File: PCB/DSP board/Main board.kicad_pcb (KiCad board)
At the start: 4 copper layers, 60 x 100 mm, 195 parts, among them J201 01x06 male SMD, J701 Conn_01x40_Female, J702 Conn_01x06_Female, J801 1140084168, J901 USB_B, U201 STM32H743II, U401 AS4C32M8SA, U501 CS42448, U601 MIC23050, U602 TPS2113A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

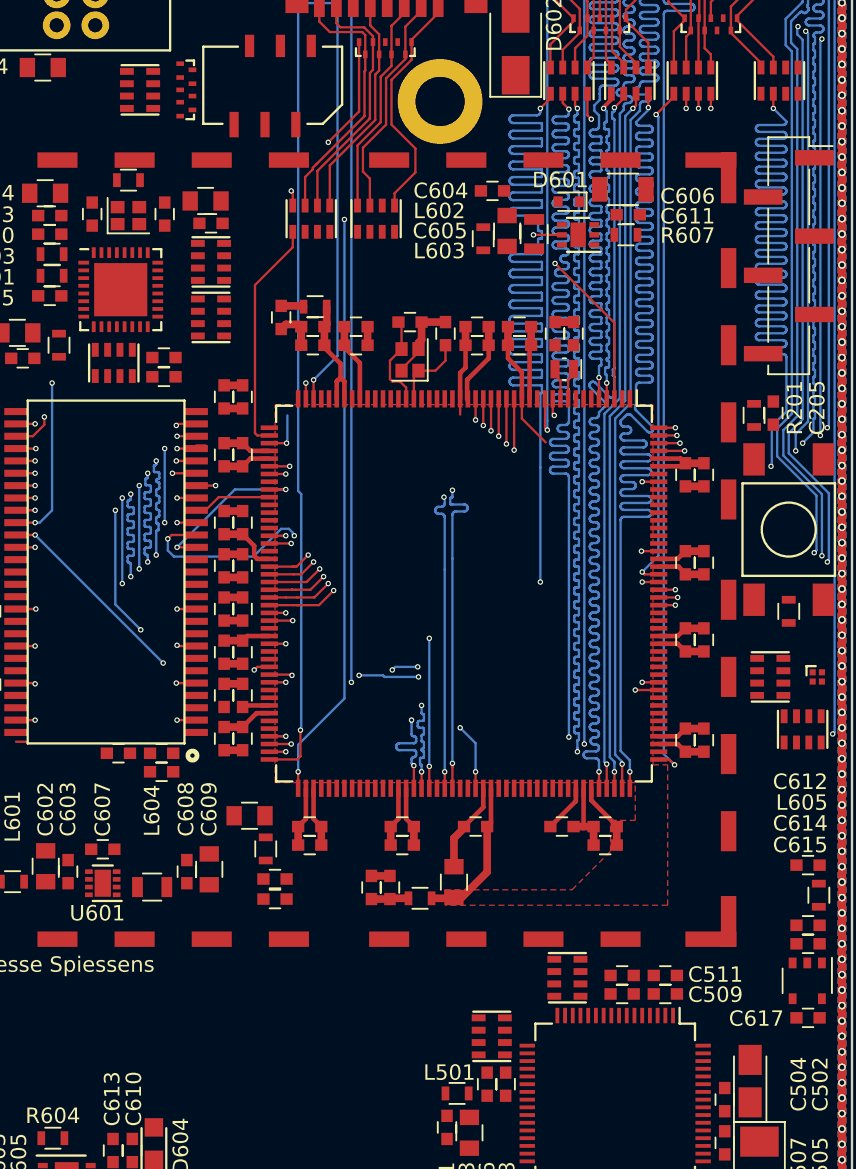
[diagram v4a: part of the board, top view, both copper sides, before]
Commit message: High Speed routing
High speed routing (USB, SDMMC, CODEC, RAM and Screen) are hooked up
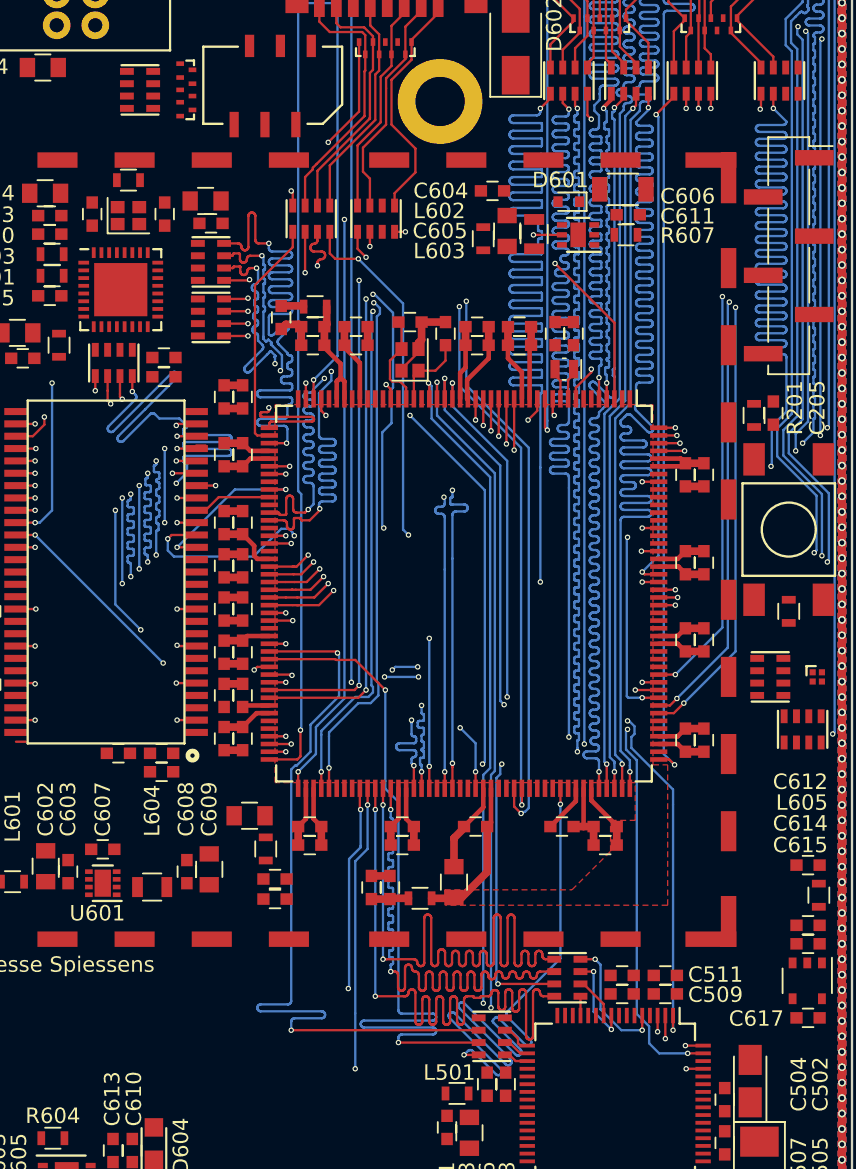
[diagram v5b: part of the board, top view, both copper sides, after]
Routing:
- net SPI5_MISO: track 0.00 -> 58.1 mm, vias 0 -> 3
- net SPI5_MOSI: track 0.00 -> 57.5 mm, vias 0 -> 3
- net SPI5_SCK: track 0.00 -> 57.5 mm, vias 0 -> 4
- net SDMMC1_D1: track 0.00 -> 55.0 mm, vias 0 -> 3
- net SDMMC1_D3: track 0.00 -> 54.7 mm, vias 0 -> 3
- net SDMMC1_CMD: track 0.00 -> 54.7 mm, vias 0 -> 3
- net SDMMC1_D2: track 0.00 -> 54.7 mm, vias 0 -> 3
- net SDMMC1_D0: track 0.00 -> 54.6 mm, vias 0 -> 3
- net SPI5_NSS: track 0.00 -> 53.7 mm, vias 0 -> 4
- net SAI2_FS_B: track 0.00 -> 50.7 mm, vias 0 -> 2
- net SAI2_FS_A: track 0.00 -> 50.7 mm, vias 0 -> 2
- net SAI2_MCK_B: track 0.00 -> 50.7 mm, vias 0 -> 5
- net SAI2_SCK_B: track 0.00 -> 50.7 mm, vias 0 -> 2
- net SAI2_SD_B: track 0.00 -> 50.7 mm, vias 0 -> 2
- net SAI2_SD_A: track 0.00 -> 50.5 mm, vias 0 -> 2
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
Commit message: PCI almost routed
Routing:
- net ADC123_INP11: track 0.00 -> 84.0 mm, vias 0 -> 8
- net ADC1_INP16: track 0.00 -> 83.7 mm, vias 0 -> 7
- net ADC3_INP6: track 0.00 -> 80.5 mm, vias 0 -> 7
- net COMP_1_INP: track 0.00 -> 76.3 mm, vias 0 -> 6
- net COMP_1_OUT: track 0.00 -> 75.4 mm, vias 0 -> 5
- net DAC1_OUT1: track 1.32 -> 76.5 mm, vias 1 -> 9
- net ADC12_INP3: track 0.00 -> 66.5 mm, vias 0 -> 2
- net HRTIM_EEV3: track 0.00 -> 62.9 mm, vias 0 -> 12
- net HRTIM_FLT3: track 0.00 -> 61.2 mm, vias 0 -> 8
- net MCO1: track 0.00 -> 53.7 mm, vias 0 -> 6
- net SPI2_SCK: track 0.00 -> 51.7 mm, vias 0 -> 5
- net HRTIM_CHE1: track 0.00 -> 44.1 mm, vias 0 -> 4
- net NRST: track 0.00 -> 40.1 mm, vias 0 -> 3
- net SPI2_MOSI: track 0.00 -> 39.7 mm, vias 0 -> 5
- net SPDIFRX_IN1: track 0.00 -> 39.4 mm, vias 0 -> 2
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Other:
- rule via_min_size: 0.3524 -> 0.35

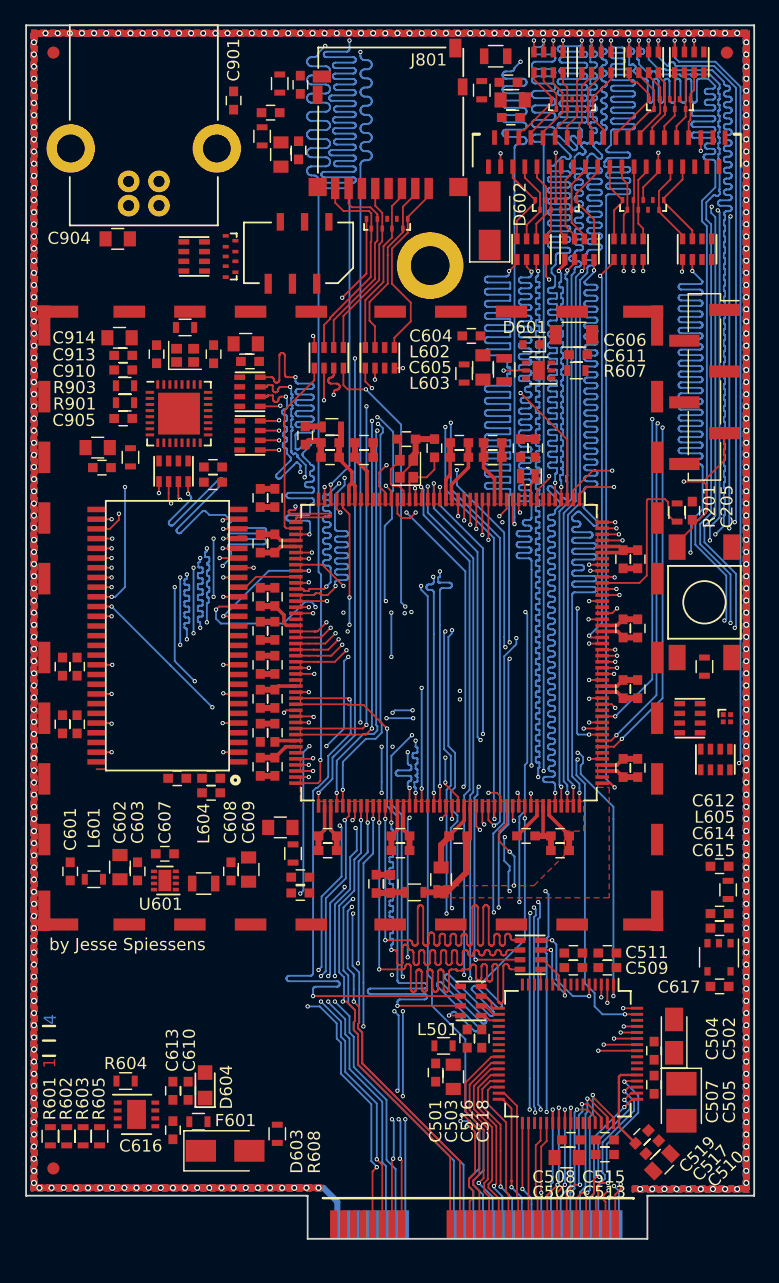
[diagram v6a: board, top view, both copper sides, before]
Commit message: Almost done routing
20 connections to be made.
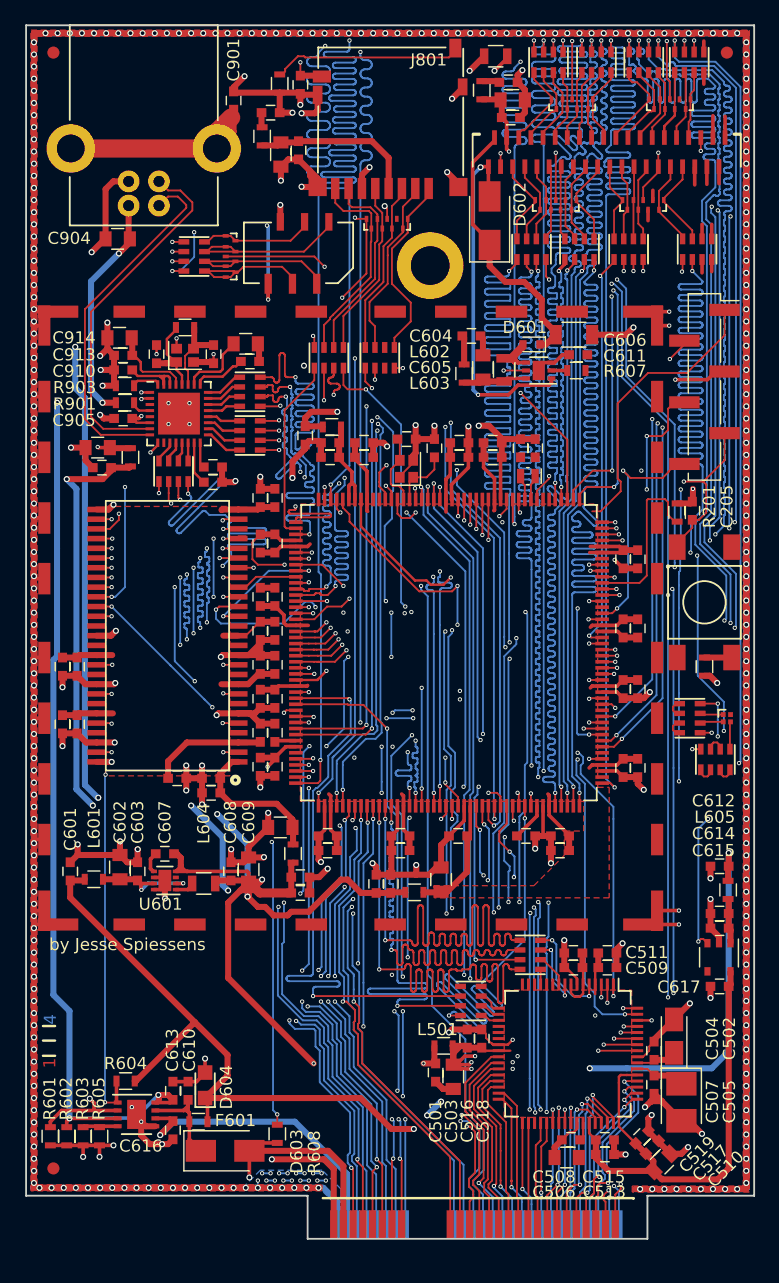
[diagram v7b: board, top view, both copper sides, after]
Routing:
- net GND: track 928.5 -> 1256.2 mm, vias 285 -> 406
- net +3V3: track 3.89 -> 212.3 mm, vias 0 -> 13
- net VBUS: track 0.00 -> 121.2 mm, vias 0 -> 6
- net +5V: track 0.00 -> 102.0 mm, vias 0 -> 5
- net I2C4_SDA: track 1.18 -> 92.7 mm, vias 1 -> 6
- net I2C4_SCL: track 1.43 -> 89.8 mm, vias 1 -> 4
- net I2C1_SCL: track 1.05 -> 75.1 mm, vias 1 -> 5
- net I2C1_SDA: track 0.97 -> 73.3 mm, vias 1 -> 4
- net TOUCH_NRESET: track 3.53 -> 61.5 mm, vias 1 -> 3
- net SPI2_NSS: track 1.11 -> 58.8 mm, vias 1 -> 4
- net TOUCH_NINT: track 4.64 -> 59.8 mm, vias 1 -> 3
- net USART6_RX: track 1.59 -> 54.1 mm, vias 1 -> 3
- net USART6_TX: track 2.10 -> 54.1 mm, vias 1 -> 4
- net PROG_IO: track 1.02 -> 50.5 mm, vias 1 -> 5
- net PROG_CLK: track 1.07 -> 50.3 mm, vias 1 -> 5
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- added copper zone on F.Cu, net +3V3_CODEC
- added copper zone on F.Cu, net +3V3_RAM
